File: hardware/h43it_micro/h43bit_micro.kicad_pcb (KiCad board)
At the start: 2 copper layers, 40 x 40 mm, 25 parts, among them J1 Conn_01x04_Pin, SW1 SW_Push, U1 ATtiny414-SS

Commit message: first draft of a finished pcb
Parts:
- added SW2: SW_Push, MyLib:FSM2JSMAATR, F.Cu at (101.3, 106.4)
- U1: footprint MyLib:SOIC-14_3.9x8.7mm_P1.27mm -> Package_SO:SOIC-14_3.9x8.7mm_P1.27mm
- moved C1 1.41 mm to (101.0, 90.7)
- moved SW1 0.92 mm to (101.3, 109.0)
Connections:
- U1 pad 3: unconnected-(U1-PA5-Pad3) -> /D+
- U1 pad 4: /D+ -> /C+
- U1 pad 6: /C+ -> unconnected-(U1-PB3-Pad6)
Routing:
- net /SW: track 6.00 -> 24.9 mm
- net /C+: track 13.8 -> 17.4 mm
- net /D+: track 13.8 -> 11.9 mm
- net VCC: track 42.2 -> 43.9 mm
- net /B+: track 9.49 -> 10.5 mm
- net GND: vias 0 -> 1

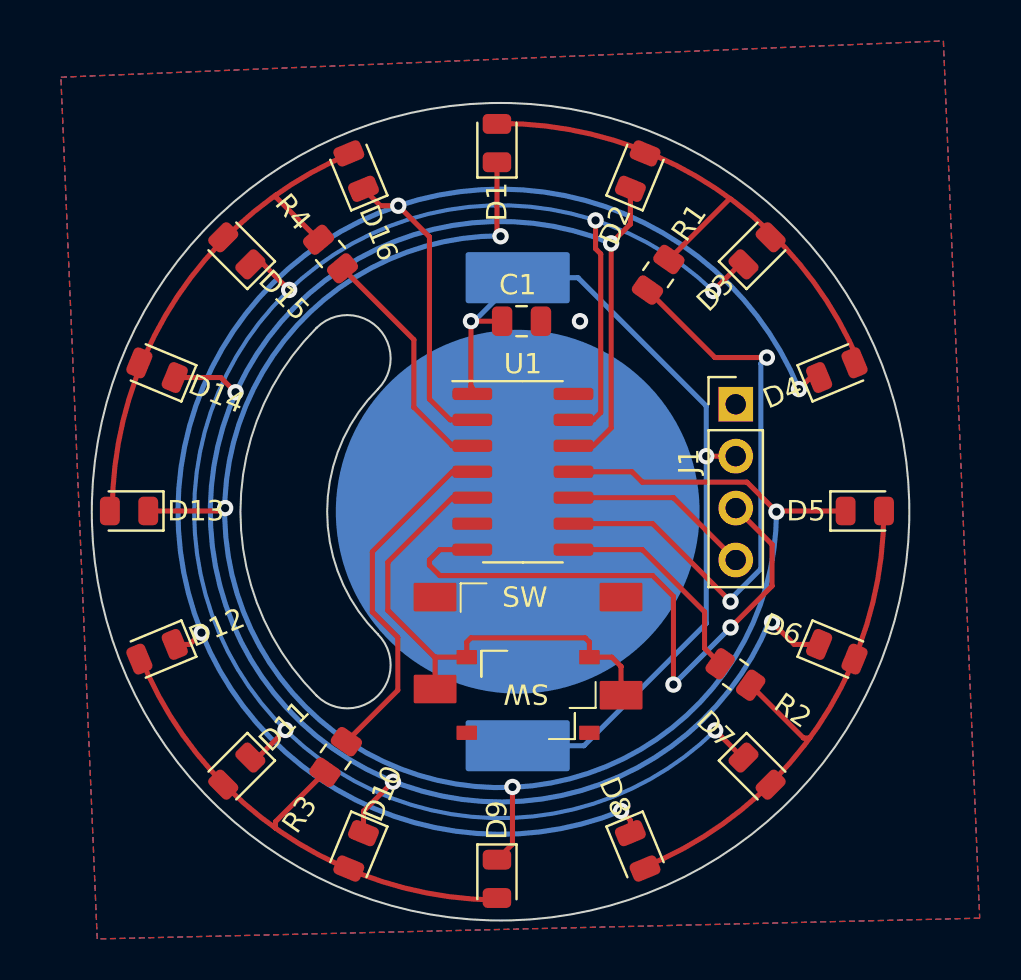
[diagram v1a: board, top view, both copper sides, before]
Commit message: add macro pcb project
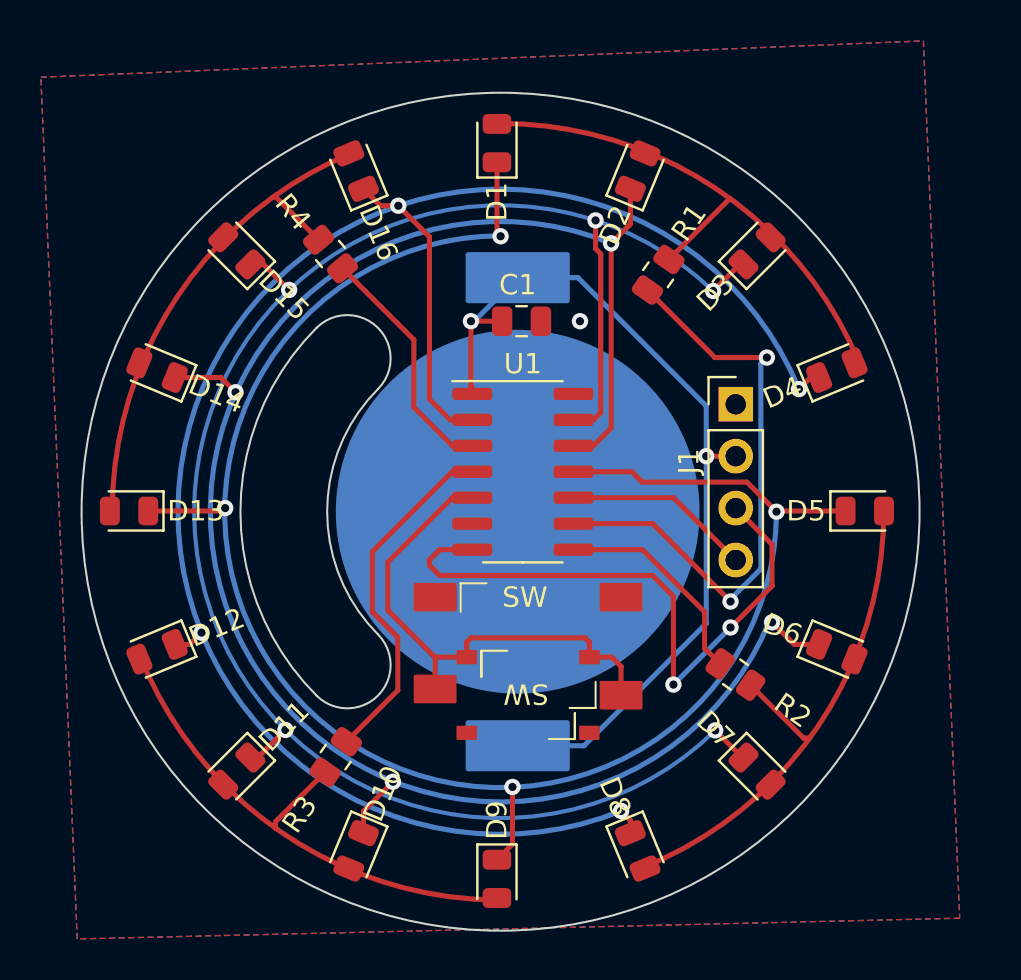
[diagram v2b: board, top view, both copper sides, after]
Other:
- board size 40 x 40 mm -> 41 x 41 mm
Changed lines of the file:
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@@
       (net 2 "/SW") (pinfunction "PA7") (pintype "bidirectional"))
     (pad "6" smd roundrect (at -2.475 2.54) (size 1.95 0.6) (layers "F.Cu" "F.Paste" "F.Mask") (roundrect_rratio 0.25)
-      (net 3 "unconnected-(U1-PB3-Pad6)") (pinfunction "PB3") (pintype "bidirectional"))
+      (net 3 "unconnected-(U1-PB3-Pad6)") (pinfunction "PB3") (pintype "bidirectional+no_connect"))
     (pad "7" smd roundrect (at -2.475 3.81) (size 1.95 0.6) (layers "F.Cu" "F.Paste" "F.Mask") (roundrect_rratio 0.25)
       (net 8 "/TX") (pinfunction "PB2") (pintype "bidirectional"))
@@
   (gr_arc (start 91 91) (mid 94 91) (end 94 94)
     (stroke (width 0.1) (type default)) (layer "Edge.Cuts"))
-  (gr_circle (center 100 100) (end 120 100)
+  (gr_circle (center 100 100) (end 120.5 100)
     (stroke (width 0.1) (type default)) (fill none) (layer "Edge.Cuts"))
   (gr_arc (start 94 106) (mid 91.514719 100) (end 94 94)
@@
     (polygon
       (pts
-        (xy 121.666 76.962)
-        (xy 123.444 119.888)
-        (xy 80.264 120.904)
-        (xy 78.486 78.74)
+        (xy 120.687559 76.962)
+        (xy 122.465559 119.888)
+        (xy 79.285559 120.904)
+        (xy 77.507559 78.74)
       )
     )

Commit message: switch SW on micro
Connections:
- U1 pad 4: /C+ -> /SW
- U1 pad 5: /SW -> /C+
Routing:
- net /SW: track 24.9 -> 29.8 mm
- net /C+: track 17.4 -> 16.7 mm
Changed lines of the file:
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@@
       (net 6 "/D+") (pinfunction "PA5") (pintype "bidirectional"))
     (pad "4" smd roundrect (at -2.475 0) (size 1.95 0.6) (layers "F.Cu" "F.Paste" "F.Mask") (roundrect_rratio 0.25)
-      (net 7 "/C+") (pinfunction "PA6") (pintype "bidirectional"))
+      (net 2 "/SW") (pinfunction "PA6") (pintype "bidirectional"))
     (pad "5" smd roundrect (at -2.475 1.27) (size 1.95 0.6) (layers "F.Cu" "F.Paste" "F.Mask") (roundrect_rratio 0.25)
-      (net 2 "/SW") (pinfunction "PA7") (pintype "bidirectional"))
+      (net 7 "/C+") (pinfunction "PA7") (pintype "bidirectional"))
     (pad "6" smd roundrect (at -2.475 2.54) (size 1.95 0.6) (layers "F.Cu" "F.Paste" "F.Mask") (roundrect_rratio 0.25)
       (net 3 "unconnected-(U1-PB3-Pad6)") (pinfunction "PB3") (pintype "bidirectional+no_connect"))
@@
     (stroke (width 0.2) (type default)) (fill none) (layer "User.5"))
   (via (at 103.886 90.678) (size 0.8) (drill 0.4) (layers "F.Cu" "B.Cu") (free) (net 1))
-  (segment (start 94.488 102.468001) (end 97.642001 99.314) (width 0.25) (layer "F.Cu") (net 2))
-  (segment (start 96.796 107.138) (end 94.488 104.83) (width 0.25) (layer "F.Cu") (net 2))
   (segment (start 96.818 107.116) (end 98.346 107.116) (width 0.25) (layer "F.Cu") (net 2))
+  (segment (start 94.488 104.83) (end 96.796 107.138) (width 0.25) (layer "F.Cu") (net 2))
+  (segment (start 100.076 98.806) (end 100.076 99.568) (width 0.25) (layer "F.Cu") (net 2))
   (segment (start 104.14 106.172) (end 98.552 106.172) (width 0.25) (layer "F.Cu") (net 2))
-  (segment (start 94.488 104.83) (end 94.488 102.468001) (width 0.25) (layer "F.Cu") (net 2))
   (segment (start 104.346 106.378) (end 104.14 106.172) (width 0.25) (layer "F.Cu") (net 2))
   (segment (start 105.896 107.5724) (end 105.896 108.976) (width 0.25) (layer "F.Cu") (net 2))
+  (segment (start 99.314 98.044) (end 100.076 98.806) (width 0.25) (layer "F.Cu") (net 2))
+  (segment (start 98.617 98.044) (end 99.314 98.044) (width 0.25) (layer "F.Cu") (net 2))
   (segment (start 98.552 106.172) (end 98.346 106.378) (width 0.25) (layer "F.Cu") (net 2))
-  (segment (start 97.642001 99.314) (end 98.617 99.314) (width 0.25) (layer "F.Cu") (net 2))
+  (segment (start 100.076 99.568) (end 99.705 99.939) (width 0.25) (layer "F.Cu") (net 2))
   (segment (start 104.346 107.116) (end 105.4396 107.116) (width 0.25) (layer "F.Cu") (net 2))
+  (segment (start 99.705 99.939) (end 97.017001 99.939) (width 0.25) (layer "F.Cu") (net 2))
   (segment (start 98.346 106.378) (end 98.346 107.116) (width 0.25) (layer "F.Cu") (net 2))
+  (segment (start 94.488 102.468001) (end 94.488 104.83) (width 0.25) (layer "F.Cu") (net 2))
   (segment (start 104.346 107.116) (end 104.346 106.378) (width 0.25) (layer "F.Cu") (net 2))
   (segment (start 105.4396 107.116) (end 105.896 107.5724) (width 0.25) (layer "F.Cu") (net 2))
   (segment (start 96.796 107.138) (end 96.818 107.116) (width 0.25) (layer "F.Cu") (net 2))
+  (segment (start 97.017001 99.939) (end 94.488 102.468001) (width 0.25) (layer "F.Cu") (net 2))
+  (segment (start 97.642001 98.044) (end 98.617 98.044) (width 0.25) (layer "F.Cu") (net 2))
   (segment (start 96.796 108.676) (end 96.796 107.138) (width 0.25) (layer "F.Cu") (net 2))
   (segment (start 98.552 93.886439) (end 98.617 93.951439) (width 0.25) (layer "F.Cu") (net 4))
@@
   (segment (start 95.758 94.889999) (end 95.758 91.582384) (width 0.25) (layer "F.Cu") (net 6))
   (segment (start 92.26602 88.090404) (end 95.758 91.582384) (width 0.25) (layer "F.Cu") (net 6))
-  (segment (start 93.726 104.902) (end 93.726 101.960001) (width 0.25) (layer "F.Cu") (net 7))
+  (segment (start 96.52 99.314) (end 98.617 99.314) (width 0.25) (layer "F.Cu") (net 7))
   (segment (start 94.971 108.737) (end 94.971 106.147) (width 0.25) (layer "F.Cu") (net 7))
+  (segment (start 93.726 104.902) (end 93.726 102.108) (width 0.25) (layer "F.Cu") (net 7))
   (segment (start 92.456 111.252) (end 94.971 108.737) (width 0.25) (layer "F.Cu") (net 7))
+  (segment (start 93.726 102.108) (end 96.52 99.314) (width 0.25) (layer "F.Cu") (net 7))
   (segment (start 94.971 106.147) (end 93.726 104.902) (width 0.25) (layer "F.Cu") (net 7))
-  (segment (start 93.726 101.960001) (end 97.642001 98.044) (width 0.25) (layer "F.Cu") (net 7))
-  (segment (start 97.642001 98.044) (end 98.617 98.044) (width 0.25) (layer "F.Cu") (net 7))
   (segment (start 97.028 103.124) (end 107.442 103.124) (width 0.25) (layer "F.Cu") (net 8))
   (segment (start 108.458 104.14) (end 108.458 108.458) (width 0.25) (layer "F.Cu") (net 8))
